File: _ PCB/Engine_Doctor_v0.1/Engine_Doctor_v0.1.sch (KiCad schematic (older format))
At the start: 2 parts

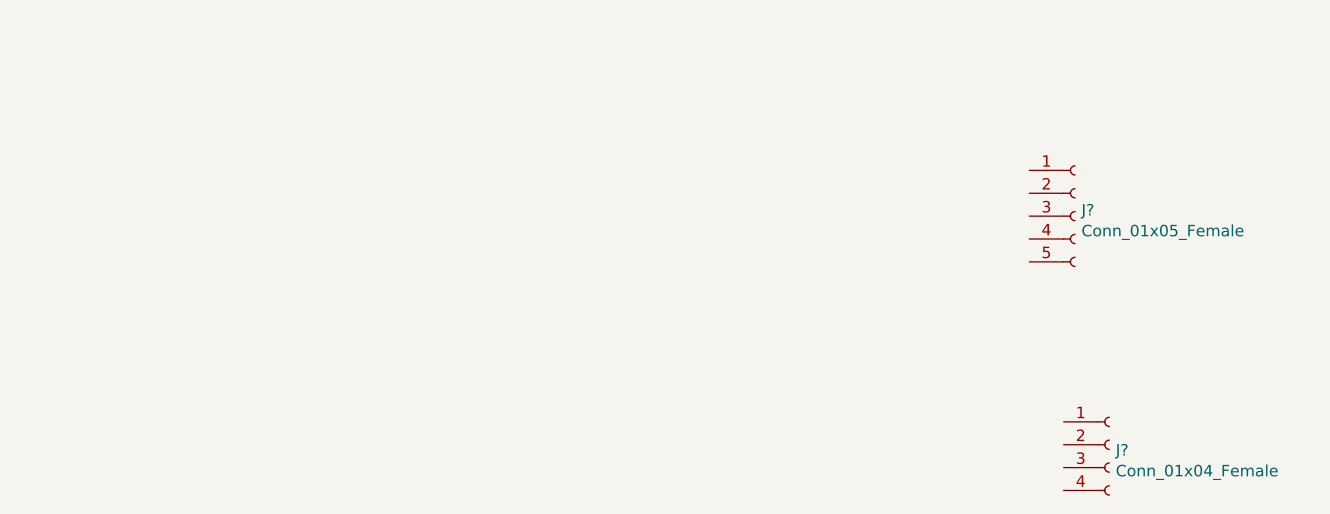
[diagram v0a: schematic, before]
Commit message: Updated with Lolin board files
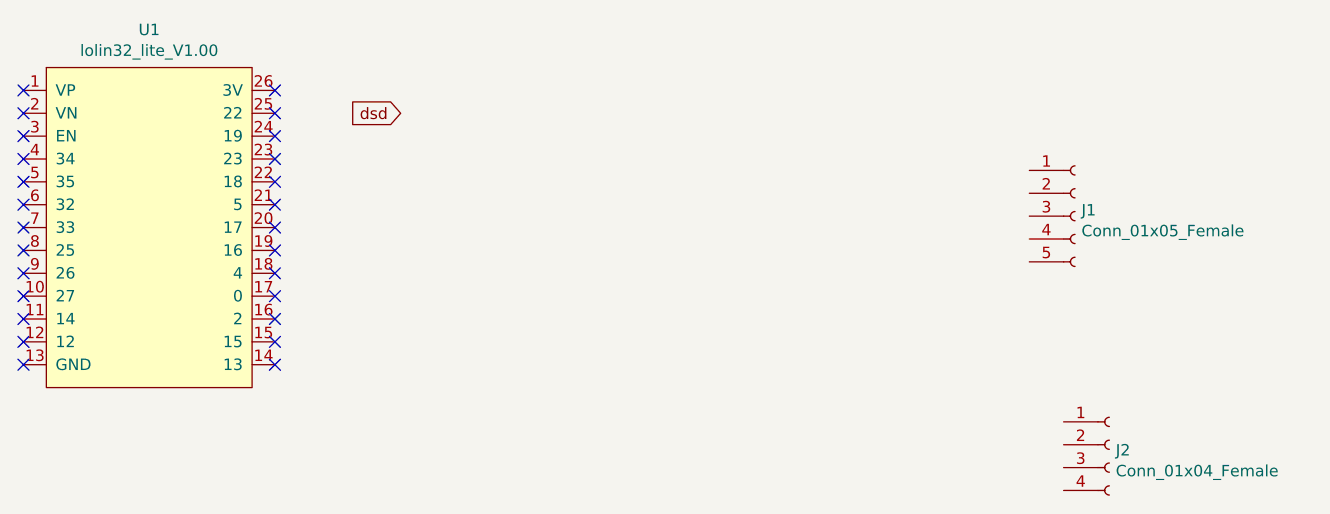
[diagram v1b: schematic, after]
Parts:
- added U1: lolin32_lite_V1.00, lolin32:lolin32_lite, symbol LOLIN32:lolin32_lite_V1.00
- gave numbers to parts that had none: 2
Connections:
- no-connect marks 0 -> 26
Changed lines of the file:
@@
 $EndDescr
 $Comp
-L Connector:Conn_01x05_Female J?
+L Connector:Conn_01x05_Female J1
 U 1 1 607ED4FA
 P 8500 2900
-F 0 "J?" H 8528 2926 50  0000 L CNN
+F 0 "J1" H 8528 2926 50  0000 L CNN
 F 1 "Conn_01x05_Female" H 8528 2835 50  0000 L CNN
 F 2 "" H 8500 2900 50  0001 C CNN
@@
 $EndComp
 $Comp
-L Connector:Conn_01x04_Female J?
+L Connector:Conn_01x04_Female J2
 U 1 1 607EDFB4
 P 8650 3900
-F 0 "J?" H 8678 3876 50  0000 L CNN
+F 0 "J2" H 8678 3876 50  0000 L CNN
 F 1 "Conn_01x04_Female" H 8678 3785 50  0000 L CNN
 F 2 "" H 8650 3900 50  0001 C CNN
@@
 	1    0    0    -1
 $EndComp
+$Comp
+L LOLIN32:lolin32_lite_V1.00 U1
+U 1 1 6082C592
+P 4450 2950
+F 0 "U1" H 4450 3815 50  0000 C CNN
+F 1 "lolin32_lite_V1.00" H 4450 3724 50  0000 C CNN
+F 2 "lolin32:lolin32_lite" H 4050 3700 50  0001 C CNN
+F 3 "" H 4050 3700 50  0001 C CNN
+	1    4450 2950
+	1    0    0    -1
+$EndComp
+Text GLabel 5550 2450 0    50   Input ~ 0
+dsd
+NoConn ~ 5000 2350
+NoConn ~ 5000 2450
+NoConn ~ 5000 2550
+NoConn ~ 5000 2650
+NoConn ~ 5000 2750
+NoConn ~ 5000 2850
+NoConn ~ 5000 2950
+NoConn ~ 5000 3050
+NoConn ~ 5000 3150
+NoConn ~ 5000 3250
+NoConn ~ 5000 3350
+NoConn ~ 5000 3450
+NoConn ~ 5000 3550
+NoConn ~ 3900 3550
+NoConn ~ 3900 3450
+NoConn ~ 3900 3350
+NoConn ~ 3900 3250
+NoConn ~ 3900 3150
+NoConn ~ 3900 3050
+NoConn ~ 3900 2950
+NoConn ~ 3900 2850
+NoConn ~ 3900 2750
+NoConn ~ 3900 2650
+NoConn ~ 3900 2550
+NoConn ~ 3900 2450
+NoConn ~ 3900 2350
 $EndSCHEMATC
